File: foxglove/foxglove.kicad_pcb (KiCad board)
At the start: 2 copper layers, 70.7 x 53.3 mm, 19 parts, among them J1 NEIGHBOR1, J2 NEIGHBOR2, J3 RJ45, J7 BONUS_ROW, P1 CONN_02X05, U1 SHIFTER1, U10 iCE40HX4K, U2 SHIFTER2, U3 SHIFTER3, U4 SHIFTER4, U5 SHIFTER5, U6 SHIFTER6, U7 SHIFTER7, U8 SHIFTER8, U9 SLG46621

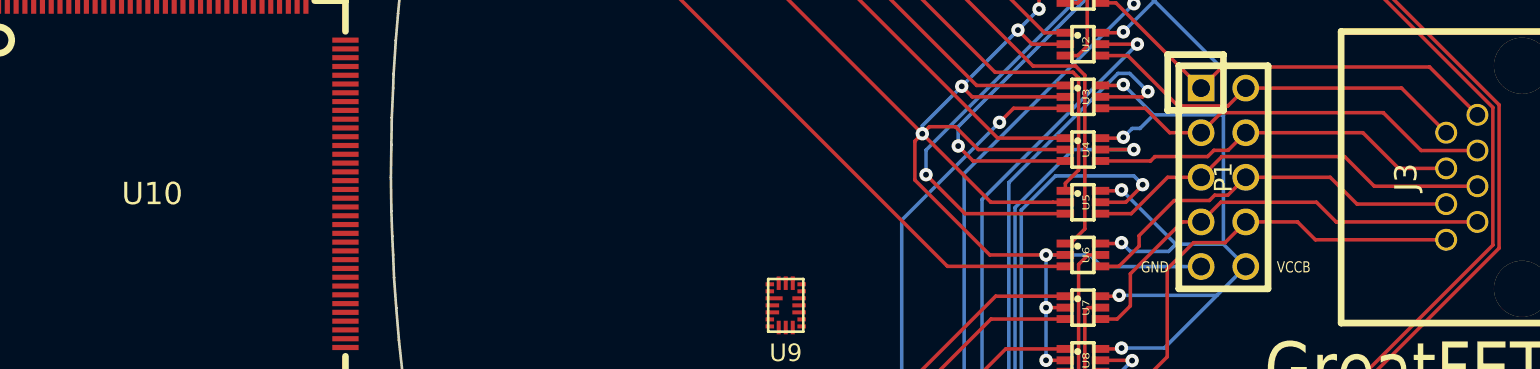
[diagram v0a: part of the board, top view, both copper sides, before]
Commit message: Added iCE40-HX8K-CT256 to schematic, began signal routing.
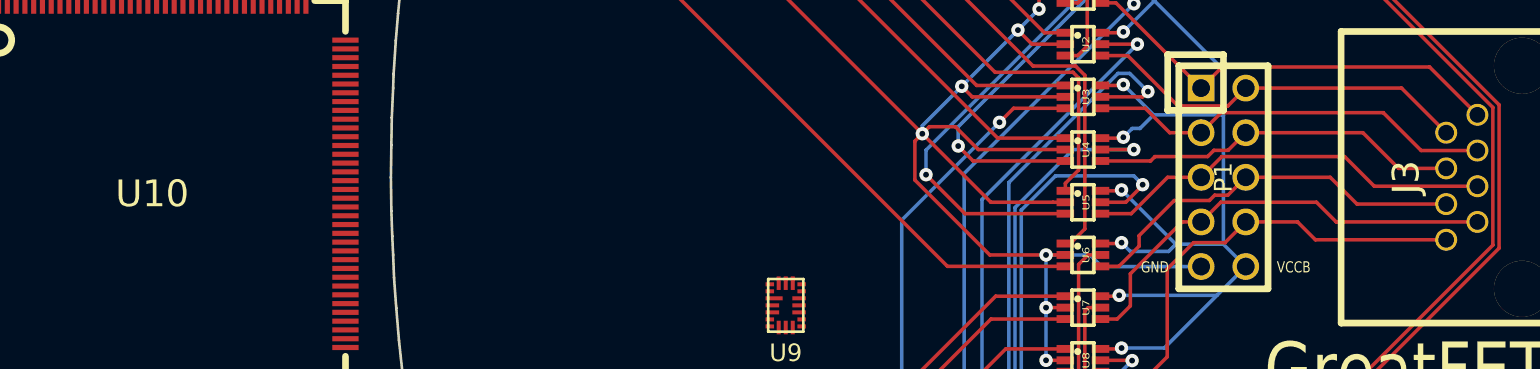
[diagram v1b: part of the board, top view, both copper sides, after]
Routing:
- added copper zone on In1.Cu, net GND
- added copper zone on In2.Cu, net VCC
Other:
- copper layers 2 -> 4
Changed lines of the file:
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@@
-(kicad_pcb (version 4) (host pcbnew 4.0.7-e2-6376~61~ubuntu18.04.1)
+(kicad_pcb (version 20171130) (host pcbnew 5.0.2-bee76a0~70~ubuntu18.04.1)
   (general
-    (links 96)
-    (no_connects 2)
-    (area 109.525999 68.504999 180.415001 121.995001)
     (thickness 1.6)
     (drawings 122)
@@
   (layers
     (0 F.Cu signal)
+    (1 In1.Cu mixed)
+    (2 In2.Cu mixed)
     (31 B.Cu signal)
     (32 B.Adhes user)
@@
     (pad_drill 0.762)
     (pad_to_mask_clearance 0.127)
+    (solder_mask_min_width 0.25)
     (pad_to_paste_clearance_ratio -0.05)
     (aux_axis_origin 0 0)
@@
       (layerselection 0x010e8_80000001)
       (usegerberextensions true)
+      (usegerberattributes false)
+      (usegerberadvancedattributes false)
+      (creategerberjobfile false)
       (excludeedgelayer true)
       (linewidth 0.100000)
@@
       (hpglpennumber 1)
       (hpglpenspeed 20)
-      (hpglpendiameter 15)
-      (hpglpenoverlay 2)
+      (hpglpendiameter 15.000000)
       (psnegative false)
       (psa4output false)
@@
       (drillshape 0)
       (scaleselection 1)
-      (outputdirectory gerber))
+      (outputdirectory "gerber"))
   )
   (net 0 "")
@@
     (at 174 95.58 90)
     (fp_text reference J3 (at 0 -6.6 90) (layer F.SilkS)
-      (effects (font (thickness 0.3)))
+      (effects (font (size 1.524 1.524) (thickness 0.3)))
     )
     (fp_text value RJ45 (at 0.254 2.54 90) (layer F.SilkS) hide
-      (effects (font (thickness 0.3)))
+      (effects (font (size 1.524 1.524) (thickness 0.3)))
     )
     (fp_line (start 8.3 -10.3) (end 8.3 1.5) (layer F.SilkS) (width 0.381))
@@
     (at 96.012 96.52)
     (fp_text reference U10 (at 0 0) (layer F.SilkS)
-      (effects (font (thickness 0.3048)))
+      (effects (font (size 1.524 1.524) (thickness 0.3048)))
     )
     (fp_text value iCE40HX4K (at 0 0) (layer F.SilkS) hide
-      (effects (font (thickness 0.3048)))
+      (effects (font (size 1.524 1.524) (thickness 0.3048)))
     )
     (fp_circle (center -8.7503 -8.7503) (end -8.001 -8.7503) (layer F.SilkS) (width 0.381))

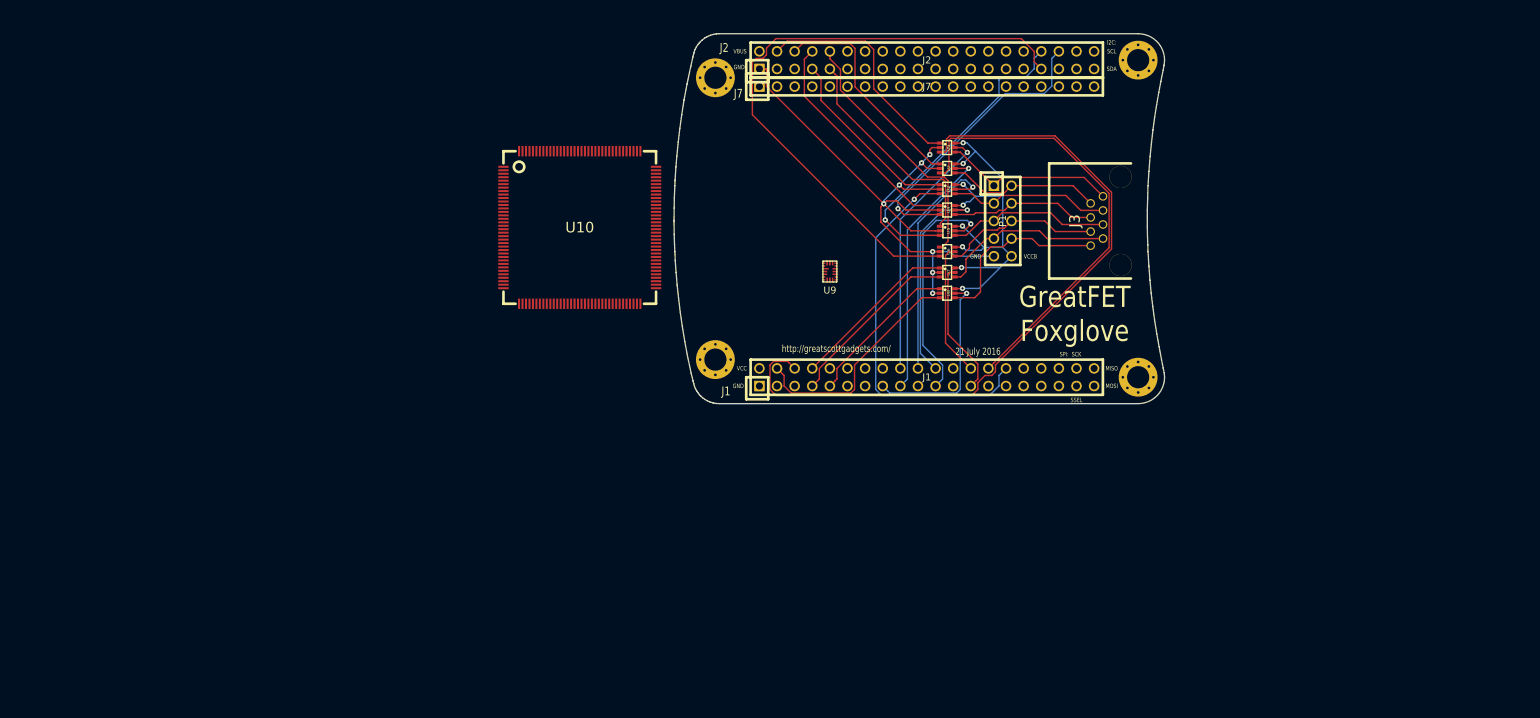
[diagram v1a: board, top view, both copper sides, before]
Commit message: Foxglove: Routed signals to FPGA and set up bank A multiplexors
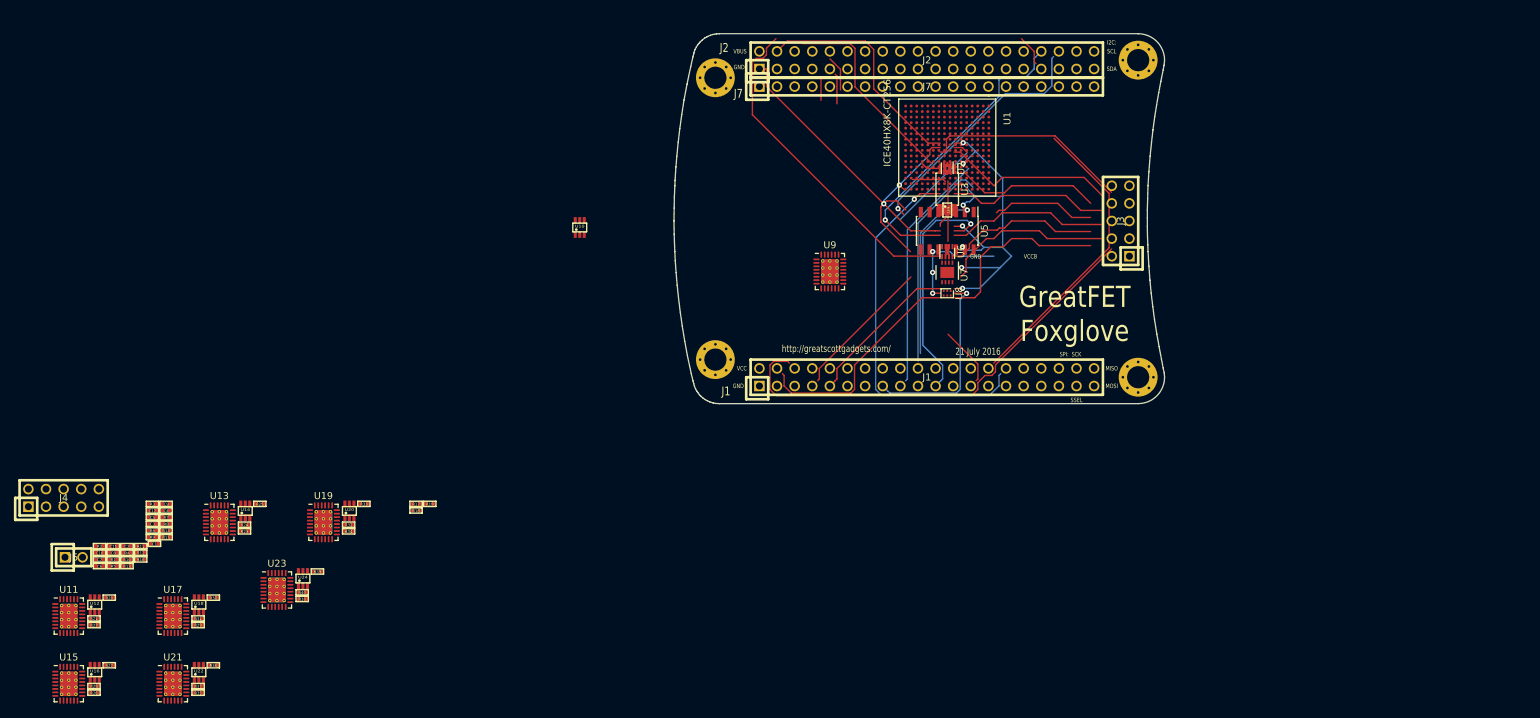
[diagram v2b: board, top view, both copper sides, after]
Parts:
- removed P1: CONN_02X05, gsg-modules:HEADER-2x5
- added C1: 10uF, gsg-modules:0402, F.Cu at (34.7, 142.1)
- added C10: 1uF, gsg-modules:0402, F.Cu at (26.8, 143.4)
- added C11: 1uF, gsg-modules:0402, F.Cu at (28.7, 142.5)
- added C12: 1uF, gsg-modules:0402, F.Cu at (34.4, 137.3)
- added C2: 100nF, gsg-modules:0402, F.Cu at (30.7, 142.5)
- added C3: 10uF, gsg-modules:0402, F.Cu at (34.4, 139.3)
- added C4: 100nF, gsg-modules:0402, F.Cu at (36.4, 137.3)
- added C5: 1uF, gsg-modules:0402, F.Cu at (34.4, 138.3)
- added C6: 1uF, gsg-modules:0402, F.Cu at (26.8, 145.3)
- added C7: 1uF, gsg-modules:0402, F.Cu at (26.8, 144.4)
- added C8: 0.1uF, gsg-modules:0402, F.Cu at (28.7, 143.4)
- added C9: 0.1uF, gsg-modules:0402, F.Cu at (36.4, 136.4)
- added J4: Conn_02x05_Odd_Even, gsg-modules:HEADER-2x5, F.Cu at (21.6, 135.5)
- added J5: Conn_01x02_Female, gsg-modules:HEADER-1x2, F.Cu at (23.1, 144.1)
- added R1: 10k, gsg-modules:0402, F.Cu at (28.7, 144.4)
- added R10: 10k, gsg-modules:0402, F.Cu at (30.7, 144.4)
- added R11: 165k, gsg-modules:0402, F.Cu at (32.7, 142.5)
- added R12: 20k, gsg-modules:0402, F.Cu at (32.7, 143.4)
- added R13: 217k, gsg-modules:0402, F.Cu at (30.7, 145.3)
- added R14: 165k, gsg-modules:0402, F.Cu at (36.4, 140.2)
- added R15: 10k, gsg-modules:0402, F.Cu at (36.4, 141.2)
- added R16: 20k, gsg-modules:0402, F.Cu at (32.7, 144.4)
- added R17: 10k, gsg-modules:0402, F.Cu at (72.4, 136.4)
- added R18: R, gsg-modules:0402, F.Cu at (72.4, 137.3)
- added R19: R, gsg-modules:0402, F.Cu at (74.4, 136.4)
- added R2: ???, gsg-modules:0402, F.Cu at (26.8, 142.5)
- added R20: 10k, gsg-modules:0402, F.Cu at (28.2, 149.9)
- added R21: R, gsg-modules:0402, F.Cu at (26.0, 152.9)
- added R22: R, gsg-modules:0402, F.Cu at (26.0, 153.9)
- added R23: 10k, gsg-modules:0402, F.Cu at (47.7, 140.3)
- added R24: R, gsg-modules:0402, F.Cu at (47.7, 139.4)
- added R25: R, gsg-modules:0402, F.Cu at (49.9, 136.4)
- added R26: 10k, gsg-modules:0402, F.Cu at (26.0, 163.6)
- added R27: R, gsg-modules:0402, F.Cu at (28.2, 159.6)
- added R28: R, gsg-modules:0402, F.Cu at (26.0, 162.6)
- added R29: 10k, gsg-modules:0402, F.Cu at (41.0, 153.9)
- added R3: 100, gsg-modules:0402, F.Cu at (34.4, 136.4)
- added R30: R, gsg-modules:0402, F.Cu at (43.2, 149.9)
- added R31: R, gsg-modules:0402, F.Cu at (41.0, 152.9)
- added R32: 10k, gsg-modules:0402, F.Cu at (62.7, 139.4)
- added R33: R, gsg-modules:0402, F.Cu at (64.9, 136.4)
- added R34: R, gsg-modules:0402, F.Cu at (62.7, 140.3)
- added R35: 10k, gsg-modules:0402, F.Cu at (41.0, 163.6)
- added R36: R, gsg-modules:0402, F.Cu at (43.2, 159.6)
- added R37: R, gsg-modules:0402, F.Cu at (41.0, 162.6)
- added R38: 10k, gsg-modules:0402, F.Cu at (56.0, 150.1)
- added R39: R, gsg-modules:0402, F.Cu at (58.2, 146.1)
- added R4: 10k, gsg-modules:0402, F.Cu at (30.7, 143.4)
- added R40: R, gsg-modules:0402, F.Cu at (56.0, 149.1)
- added R5: 10k, gsg-modules:0402, F.Cu at (28.7, 145.3)
- added R6: 100, gsg-modules:0402, F.Cu at (34.4, 140.2)
- added R7: 10k, gsg-modules:0402, F.Cu at (36.4, 138.3)
- added R8: 217k, gsg-modules:0402, F.Cu at (36.4, 139.3)
- added R9: 5k, gsg-modules:0402, F.Cu at (34.4, 141.2)
- added U11: 74HC4051, Package_DFN_QFN:VQFN-28-1EP_4x5mm_P0.5mm_EP2.55x3.55mm_ThermalVias, F.Cu at (22.3, 152.6)
- added U12: SHIFTER, gsg-modules:SOT363, F.Cu at (26.1, 150.9)
- added U13: 74HC4051, Package_DFN_QFN:VQFN-28-1EP_4x5mm_P0.5mm_EP2.55x3.55mm_ThermalVias, F.Cu at (44.0, 139.0)
- added U14: SHIFTER, gsg-modules:SOT363, F.Cu at (47.8, 137.4)
- added U15: 74HC4051, Package_DFN_QFN:VQFN-28-1EP_4x5mm_P0.5mm_EP2.55x3.55mm_ThermalVias, F.Cu at (22.3, 162.3)
- added U16: SHIFTER, gsg-modules:SOT363, F.Cu at (26.1, 160.7)
- added U17: 74HC4051, Package_DFN_QFN:VQFN-28-1EP_4x5mm_P0.5mm_EP2.55x3.55mm_ThermalVias, F.Cu at (37.3, 152.6)
- added U18: SHIFTER, gsg-modules:SOT363, F.Cu at (41.1, 150.9)
- added U19: 74HC4051, Package_DFN_QFN:VQFN-28-1EP_4x5mm_P0.5mm_EP2.55x3.55mm_ThermalVias, F.Cu at (59.1, 139.0)
- added U20: SHIFTER, gsg-modules:SOT363, F.Cu at (62.8, 137.4)
- added U21: 74HC4051, Package_DFN_QFN:VQFN-28-1EP_4x5mm_P0.5mm_EP2.55x3.55mm_ThermalVias, F.Cu at (37.3, 162.3)
- added U22: SHIFTER, gsg-modules:SOT363, F.Cu at (41.1, 160.7)
- added U23: 74HC4051, Package_DFN_QFN:VQFN-28-1EP_4x5mm_P0.5mm_EP2.55x3.55mm_ThermalVias, F.Cu at (52.4, 148.8)
- added U24: SHIFTER, gsg-modules:SOT363, F.Cu at (56.1, 147.1)
- J3: value RJ45 -> Conn_02x05_Odd_Even; footprint gsg-modules:RJ45-RJHSE-5380 -> gsg-modules:HEADER-2x5
- U1: value SHIFTER1 -> ICE40HX8K-CT256; footprint gsg-modules:SOT363 -> gsg-modules:BGA256C80P16X16_1400X1400X170
- U10: value iCE40HX4K -> SHIFTER; footprint gsg-modules:LQFP144 -> gsg-modules:SOT363
- U2: value SHIFTER2 -> TLV711; footprint gsg-modules:SOT363 -> Package_SON:WSON-6_1.5x1.5mm_P0.5mm
- U3: value SHIFTER3 -> MC4558CPT; footprint gsg-modules:SOT363 -> Package_SO:TSSOP-8_4.4x3mm_P0.65mm
- U4: value SHIFTER4 -> 74LVC1G3157
- U5: value SHIFTER5 -> LM339; footprint gsg-modules:SOT363 -> Package_SO:SOIC-14_3.9x8.7mm_P1.27mm
- U6: value SHIFTER6 -> ADP225; footprint gsg-modules:SOT363 -> Package_CSP:LFCSP-8_2x2mm_P0.5mm
- U7: value SHIFTER7 -> DAC084S085; footprint gsg-modules:SOT363 -> Package_SON:WSON-8-1EP_3x3mm_P0.5mm_EP1.6x2.0mm
- U8: value SHIFTER8 -> 74AHC1G04; footprint gsg-modules:SOT363 -> Package_TO_SOT_SMD:SOT-886
- U9: value SLG46621 -> 74HC4051; footprint gsg-modules:SLG46621 -> Package_DFN_QFN:VQFN-28-1EP_4x5mm_P0.5mm_EP2.55x3.55mm_ThermalVias
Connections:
- J1 pad 10: Net-(J1-Pad10) -> /J1.10
- J1 pad 11: Net-(J1-Pad11) -> /J1.11
- J1 pad 12: Net-(J1-Pad12) -> /J1.12
- J1 pad 13: Net-(J1-Pad13) -> /J1.13
- J1 pad 14: Net-(J1-Pad14) -> /J1.14
- J1 pad 15: /DIR8 -> /J1.15
- J1 pad 16: Net-(J1-Pad16) -> /J1.16
- J1 pad 17: /DIR2 -> /J1.17
- J1 pad 18: /DIR1 -> /J1.18
- J1 pad 19: Net-(J1-Pad19) -> /J1.19
- J1 pad 20: /DIR3 -> /J1.20
- J1 pad 21: /DIR5 -> /J1.21
- J1 pad 22: /DIR4 -> /J1.22
- J1 pad 23: Net-(J1-Pad23) -> /J1.23
- J1 pad 24: Net-(J1-Pad24) -> /J1.24
- J1 pad 25: /DIR7 -> /J1.25
- J1 pad 26: /DIR6 -> /J1.26
- J1 pad 27: Net-(J1-Pad27) -> /J1.27
- J1 pad 28: /A2 -> /J1.28
- J1 pad 29: Net-(J1-Pad29) -> /J1.29
- J1 pad 3: Net-(J1-Pad3) -> /J1.03
- J1 pad 30: /A3 -> /J1.30
- J1 pad 31: Net-(J1-Pad31) -> (no net)
- J1 pad 32: Net-(J1-Pad32) -> /J1.32
- J1 pad 33: Net-(J1-Pad33) -> /J1.33
- J1 pad 34: Net-(J1-Pad34) -> /J1.34
- J1 pad 35: Net-(J1-Pad35) -> /J1.35
- J1 pad 36: Net-(J1-Pad36) -> /J1.36
- J1 pad 37: Net-(J1-Pad37) -> /SSEL
- J1 pad 38: Net-(J1-Pad38) -> /SCK
- J1 pad 39: Net-(J1-Pad39) -> /MOSI
- J1 pad 4: /A8 -> /J1.04
- J1 pad 40: Net-(J1-Pad40) -> /MISO
- J1 pad 5: Net-(J1-Pad5) -> /J1.05
- J1 pad 6: /A1 -> /J1.06
- J1 pad 7: /A7 -> /J1.07
- J1 pad 8: /VA7 -> /J1.08
- J1 pad 9: /VA8 -> /J1.09
- J2 pad 10: /VA6 -> /J2.10
- J2 pad 11: Net-(J2-Pad11) -> /J2.11
- J2 pad 12: Net-(J2-Pad12) -> /J2.12
- J2 pad 13: Net-(J2-Pad13) -> /J2.13
- J2 pad 14: Net-(J2-Pad14) -> /J2.14
- J2 pad 15: Net-(J2-Pad15) -> /J2.15
- J2 pad 16: Net-(J2-Pad16) -> /J2.16
- J2 pad 17: Net-(J2-Pad17) -> /J2.17
- J2 pad 18: Net-(J2-Pad18) -> /J2.18
- J2 pad 19: Net-(J2-Pad19) -> /J2.19
- J2 pad 2: Net-(J2-Pad2) -> +5V
- J2 pad 20: Net-(J2-Pad20) -> /J2.20
- J2 pad 21: Net-(J2-Pad21) -> /J2.21
- J2 pad 22: Net-(J2-Pad22) -> /J2.22
- J2 pad 23: Net-(J2-Pad23) -> /J2.23
- J2 pad 24: Net-(J2-Pad24) -> /J2.24
- J2 pad 25: Net-(J2-Pad25) -> /J2.25
- J2 pad 26: Net-(J2-Pad26) -> /J2.26
- J2 pad 27: Net-(J2-Pad27) -> /J2.27
- J2 pad 28: Net-(J2-Pad28) -> /J2.28
- J2 pad 29: Net-(J2-Pad29) -> /J2.29
- J2 pad 3: Net-(J2-Pad3) -> /J2.03
- J2 pad 30: Net-(J2-Pad30) -> /J2.30
- J2 pad 31: Net-(J2-Pad31) -> /J2.31
- J2 pad 32: Net-(J2-Pad32) -> /J2.32
- J2 pad 33: /A6 -> /J2.33
- J2 pad 34: /A5 -> /J2.34
- J2 pad 35: Net-(J2-Pad35) -> /J2.35
- J2 pad 36: /A4 -> /J2.36
- J2 pad 37: Net-(J2-Pad37) -> /J2.37
- J2 pad 38: Net-(J2-Pad38) -> /J2.38
- J2 pad 39: Net-(J2-Pad39) -> /J2.39
- J2 pad 4: /VA1 -> /J2.04
- J2 pad 40: Net-(J2-Pad40) -> /J2.40
- J2 pad 5: Net-(J2-Pad5) -> /ADC
- J2 pad 6: /VA2 -> /J2.06
- J2 pad 7: /VA3 -> /J2.07
- J2 pad 8: /VA4 -> /J2.08
- J2 pad 9: /VA5 -> /J2.09
- J3 pad 1: /B1 -> /A1
- J3 pad 2: /B2 -> /A2
- J3 pad 3: /B3 -> /A3
- J3 pad 4: /B4 -> /A4
- J3 pad 5: /B5 -> /A5
- J3 pad 6: /B6 -> /A6
- J3 pad 7: /B7 -> /A7
- J3 pad 8: /B8 -> /A8
- J7 pad 1: Net-(J7-Pad1) -> (no net)
- J7 pad 10: Net-(J7-Pad10) -> (no net)
- J7 pad 11: Net-(J7-Pad11) -> (no net)
- J7 pad 12: Net-(J7-Pad12) -> (no net)
- J7 pad 13: Net-(J7-Pad13) -> (no net)
- J7 pad 14: Net-(J7-Pad14) -> (no net)
- J7 pad 15: Net-(J7-Pad15) -> (no net)
- J7 pad 16: Net-(J7-Pad16) -> (no net)
- J7 pad 17: Net-(J7-Pad17) -> (no net)
- J7 pad 18: Net-(J7-Pad18) -> (no net)
- J7 pad 19: Net-(J7-Pad19) -> (no net)
- J7 pad 2: Net-(J7-Pad2) -> (no net)
- J7 pad 20: Net-(J7-Pad20) -> (no net)
- J7 pad 3: Net-(J7-Pad3) -> (no net)
- J7 pad 4: Net-(J7-Pad4) -> (no net)
- J7 pad 5: Net-(J7-Pad5) -> (no net)
- J7 pad 6: Net-(J7-Pad6) -> (no net)
- J7 pad 7: Net-(J7-Pad7) -> (no net)
- J7 pad 8: Net-(J7-Pad8) -> (no net)
- J7 pad 9: Net-(J7-Pad9) -> (no net)
- U10 pad 1: Net-(U10-Pad1) -> VCC
- U10 pad 2: Net-(U10-Pad2) -> GND
- U10 pad 3: Net-(U10-Pad3) -> /A1_shift
- U10 pad 5: Net-(U10-Pad5) -> /DIR_1
- U10 pad 6: Net-(U10-Pad6) -> /VCCA
- U2 pad 1: /VA2 -> +5V
- U2 pad 2: GND -> +5V
- U2 pad 3: /A2 -> +5V
- U2 pad 4: /B2 -> GND
- U2 pad 5: /DIR2 -> +2V5
- U2 pad 6: /VCCB -> +1V2
- U3 pad 1: /VA3 -> /DAC3
- U3 pad 2: GND -> /DAC3
- U3 pad 3: /A3 -> Net-(U3-Pad3)
- U3 pad 4: /B3 -> GND
- U3 pad 5: /DIR3 -> Net-(U3-Pad5)
- U3 pad 6: /VCCB -> /DAC4
- U4 pad 1: /VA4 -> /ADC
- U4 pad 3: /A4 -> Net-(R9-Pad1)
- U4 pad 4: /B4 -> /ADC_A
- U4 pad 5: /DIR4 -> VCC
- U4 pad 6: /VCCB -> Net-(R7-Pad1)
- U5 pad 1: /VA5 -> /COUT1
- U5 pad 2: GND -> /COUT2
- U5 pad 3: /A5 -> +5V
- U5 pad 4: /B5 -> /DAC2
- U5 pad 5: /DIR5 -> /COMP1
- U5 pad 6: /VCCB -> /COMP1
- U6 pad 1: /VA6 -> /VCCA_EN
- U6 pad 2: GND -> /DAC2_EN
- U6 pad 3: /A6 -> GND
- U6 pad 4: /B6 -> Net-(R11-Pad2)
- U6 pad 5: /DIR6 -> /DAC2
- U6 pad 6: /VCCB -> +5V
- U7 pad 1: /VA7 -> +5V
- U7 pad 2: GND -> Net-(R13-Pad1)
- U7 pad 3: /A7 -> Net-(R8-Pad2)
- U7 pad 4: /B7 -> Net-(U3-Pad3)
- U7 pad 5: /DIR7 -> Net-(U3-Pad5)
- U7 pad 6: /VCCB -> GND
- U8 pad 1: /VA8 -> (no net)
- U8 pad 2: GND -> /SSEL
- U8 pad 3: /A8 -> GND
- U8 pad 4: /B8 -> Net-(R15-Pad2)
- U8 pad 5: /DIR8 -> (no net)
- U8 pad 6: /VCCB -> VCC
- U9 pad 1: VCC -> /DAC2
- U9 pad 10: Net-(U9-Pad10) -> /S1_1
- U9 pad 11: GND -> /S0_1
- U9 pad 12: Net-(U9-Pad12) -> /ADC_A
- U9 pad 14: /VDD2 -> Net-(R19-Pad1)
- U9 pad 15: Net-(U9-Pad15) -> Net-(U10-Pad4)
- U9 pad 16: Net-(U9-Pad16) -> +5V
- U9 pad 17: Net-(U9-Pad17) -> (no net)
- U9 pad 18: Net-(U9-Pad18) -> (no net)
- U9 pad 19: Net-(U9-Pad19) -> (no net)
- U9 pad 2: Net-(U9-Pad2) -> /COMP1
- U9 pad 20: Net-(U9-Pad20) -> (no net)
- U9 pad 3: Net-(U9-Pad3) -> /A1
- U9 pad 4: Net-(U9-Pad4) -> /COMP2
- U9 pad 5: Net-(U9-Pad5) -> /DAC3
- U9 pad 6: Net-(U9-Pad6) -> /~E~_1
- U9 pad 7: Net-(U9-Pad7) -> GND
- U9 pad 8: Net-(U9-Pad8) -> GND
- U9 pad 9: Net-(U9-Pad9) -> /S2_1
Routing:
- net /J2.34: track 0.00 -> 44.5 mm, vias 0 -> 1
- net /A5: track 44.5 -> 0.00 mm, vias 1 -> 0
- net /A6: track 89.4 -> 53.0 mm
- net /J1.21: track 0.00 -> 34.3 mm, vias 0 -> 1
- net /DIR5: track 34.3 -> 0.00 mm, vias 1 -> 0
- net /VA1: track 33.6 -> 0.00 mm
- net /J2.04: track 0.00 -> 33.6 mm
- net /VA4: track 33.1 -> 0.00 mm
- net /J1.15: track 0.00 -> 27.9 mm, vias 0 -> 1
- net /DIR8: track 27.9 -> 0.00 mm, vias 1 -> 0
- net /VA7: track 24.5 -> 0.00 mm
- net /VA3: track 27.3 -> 3.28 mm
- net /VA6: track 37.3 -> 13.9 mm
- net /VA8: track 22.6 -> 0.00 mm
- net /J1.09: track 0.00 -> 22.6 mm
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
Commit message: Continued work on Foxglove schematic (added bypass caps, selected footprints, etc.). Placed parts on PCB.
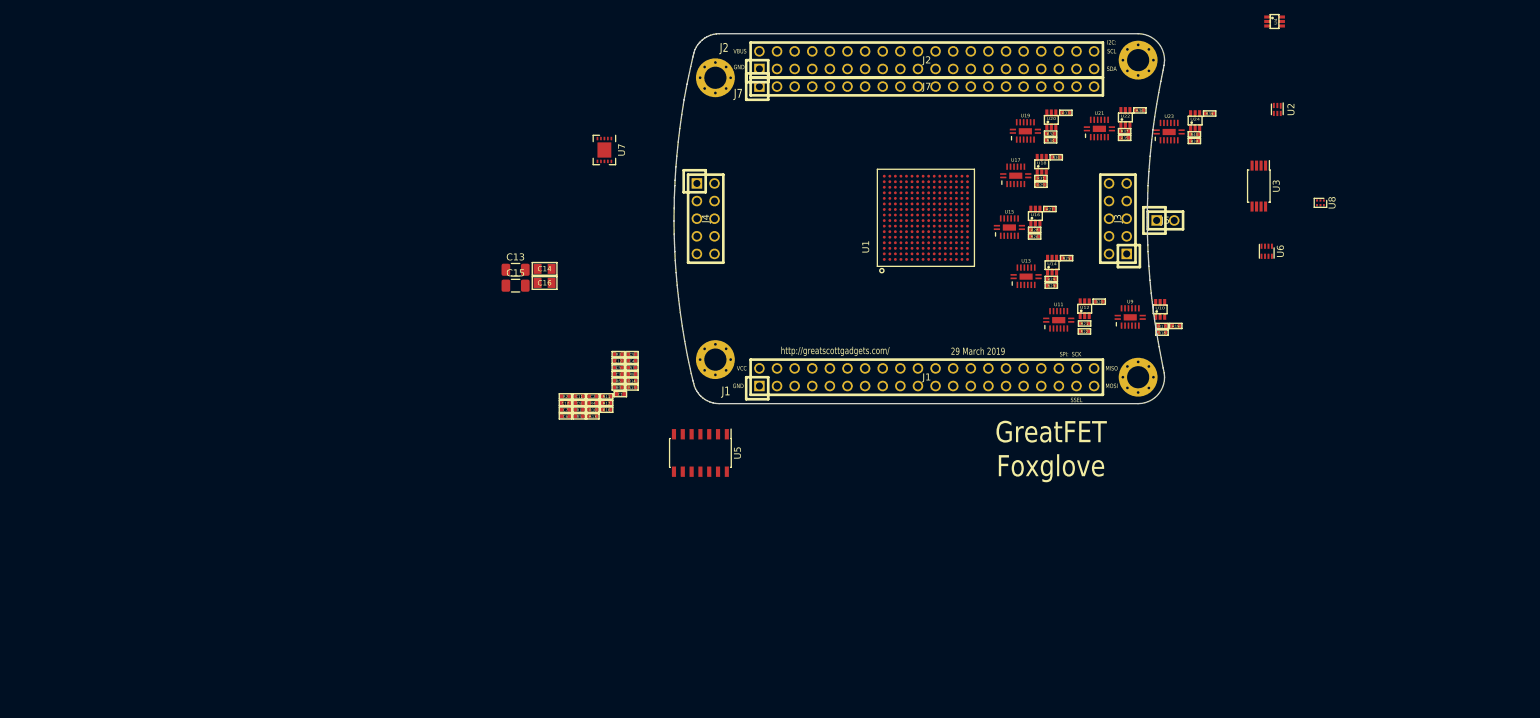
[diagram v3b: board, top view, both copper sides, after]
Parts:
- added C13: 10uF, Capacitor_SMD:C_1206_3216Metric, F.Cu at (86.8, 102.6)
- added C14: 0.1uF, gsg-modules:0805, F.Cu at (90.9, 102.5)
- added C15: 10uF, Capacitor_SMD:C_1206_3216Metric, F.Cu at (86.8, 104.9)
- added C16: 0.1uF, gsg-modules:0805, F.Cu at (90.9, 104.5)
- U11, U13, U15, U17, U19, U21, U23, U9: footprint Package_DFN_QFN:VQFN-28-1EP_4x5mm_P0.5mm_EP2.55x3.55mm_ThermalVias -> Package_TO_SOT_SMD:SOT-763-1
- U7: footprint Package_SON:WSON-8-1EP_3x3mm_P0.5mm_EP1.6x2.0mm -> Package_SON:WSON-10-1EP_4x3mm_P0.5mm_EP2.2x2mm
- moved J5 164.7 mm to (180.5, 95.5)
- moved R36 155.7 mm to (176.8, 79.6)
- moved R35 155.7 mm to (174.6, 83.6)
- moved R37 155.7 mm to (174.6, 82.6)
- moved U21 155.7 mm to (170.9, 82.3)
- moved U22 155.7 mm to (174.7, 80.7)
- moved U16 150.7 mm to (161.7, 94.9)
- moved R26 150.7 mm to (161.6, 97.8)
- moved R27 150.7 mm to (163.8, 93.9)
- moved R28 150.7 mm to (161.6, 96.9)
- moved U15 150.7 mm to (158.0, 96.5)
- moved R21 149.0 mm to (168.8, 110.4)
- moved R20 149.0 mm to (170.9, 107.2)
- moved U11 149.0 mm to (165.1, 109.9)
- moved U12 149.0 mm to (168.8, 108.2)
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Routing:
- net /A1: track 96.2 -> 0.00 mm
- net GND: track 82.2 -> 0.00 mm, vias 5 -> 0
- net /VCCB: track 61.2 -> 0.00 mm, vias 7 -> 0
- net /A3: track 54.4 -> 0.00 mm, vias 1 -> 0
- net /A6: track 53.0 -> 0.00 mm
- net /J2.34: track 44.5 -> 0.00 mm, vias 1 -> 0
- net /A2: track 42.6 -> 0.00 mm
- net /A4: track 35.7 -> 0.00 mm, vias 1 -> 0
- net /DIR2: track 34.4 -> 0.00 mm
- net /J1.21: track 34.3 -> 0.00 mm, vias 1 -> 0
- net /J2.04: track 33.6 -> 0.00 mm
- net /A8: track 32.6 -> 0.00 mm
- net /DIR3: track 30.8 -> 0.00 mm
- net /VA2: track 29.1 -> 0.00 mm
- net /J1.15: track 27.9 -> 0.00 mm, vias 1 -> 0
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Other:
- board text added: "29 March 2019"
- board text removed: "21 July 2016"
- board text removed: "VCCB"
